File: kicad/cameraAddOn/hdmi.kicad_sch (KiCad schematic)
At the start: 13 parts, among them J4 HDMI_A, U7 SII164CTG64

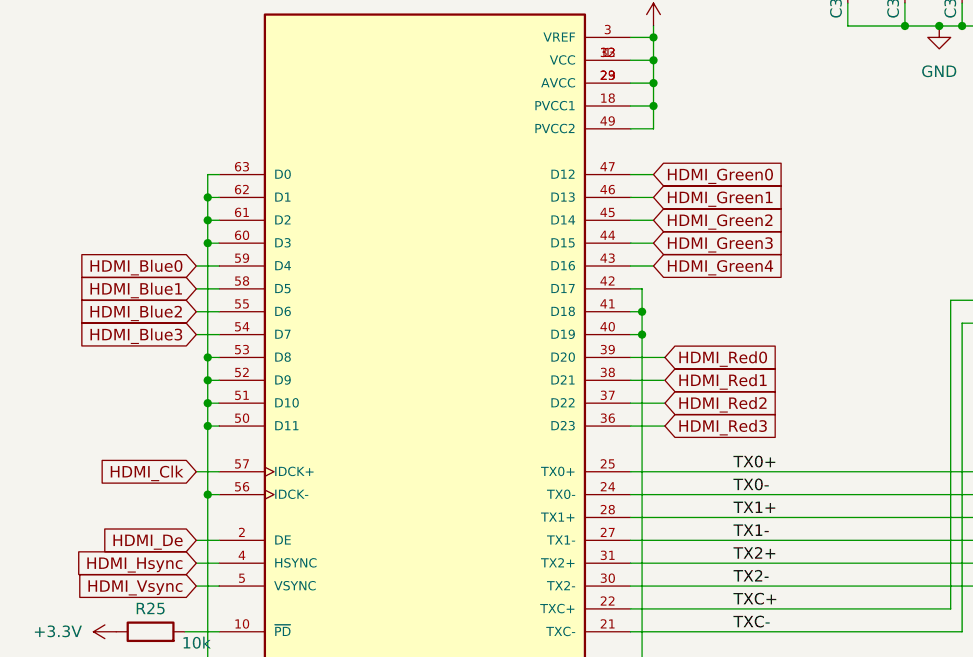
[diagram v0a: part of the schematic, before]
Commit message: V1.1 of perifAddOn (added bus-switch on sd-card)
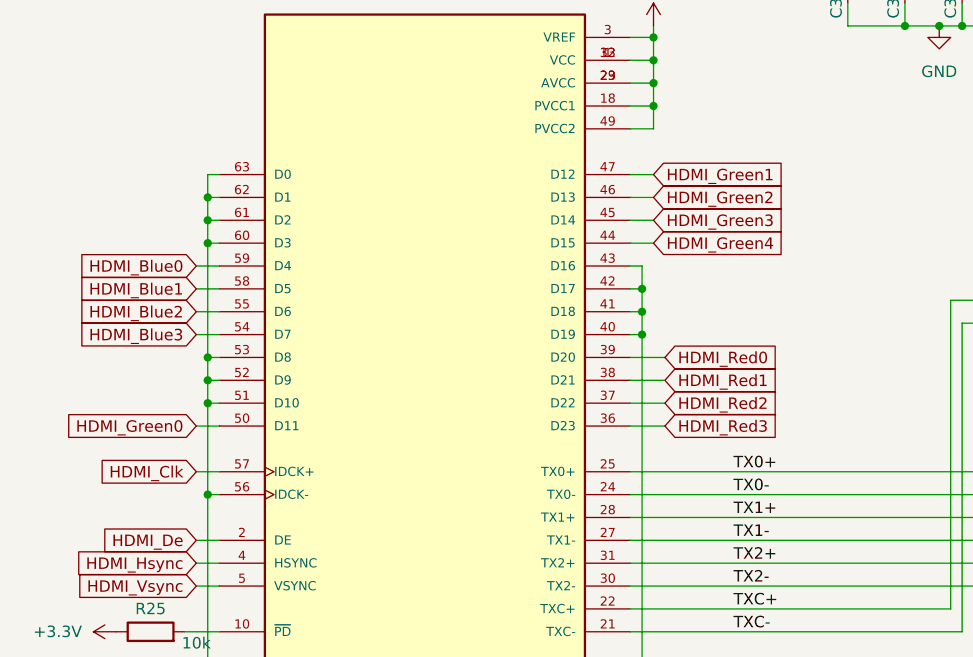
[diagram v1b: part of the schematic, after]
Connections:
- net GND: now also U7.43 (D16); no longer U7.50 (D11)
- net HDMI_Green0: now also U7.50 (D11); no longer U7.47 (D12)
- net HDMI_Green1: now also U7.47 (D12); no longer U7.46 (D13)
- net HDMI_Green2: now also U7.46 (D13); no longer U7.45 (D14)
- net HDMI_Green3: now also U7.45 (D14); no longer U7.44 (D15)
- net HDMI_Green4: now also U7.44 (D15); no longer U7.43 (D16)
